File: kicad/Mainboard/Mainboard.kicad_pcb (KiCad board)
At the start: 2 copper layers, 46.9 x 107.1 mm, 277 parts, among them J10 MIC_EXT, J11 VIB2, J12 SPK_EXT, J13 GPS_CONN, J14 Micro_SD_Card, J15 DBG_CONN, J3 USB_OTG, J4 SWD, J5 BATT, J6 POT_PWR_SW, J7 Conn_01x10, J8 Antenna, J9 VIB1, Q1 BSS138, Q2 BSS138, Q3 BGA6589, Q4 BSS138, Q5 BSS138, Q6 BSS138, Q7 FDV304P, SW1 INT_PTT_SW, T1 AFT05MS004NT1, U1 STM32F777VIT, U10 LM386, U11 LSM9DS1, U12 GD25Q16CSIGTR, U13 BGA2874, U14 ESP8266EX, U2 USBLC6-2SC6, U3 LD1117S50TR_SOT223, U4 LD1117S33TR_SOT223, U5 ADF7021, U6 HMC546MS8GETR, U7 LM2904A, U8 HEF4066B, U9 OPA340UA, X1 12.288MHz, Y1 24MHz

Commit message: few fixes
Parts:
- moved C26 1.53 mm to (44.4, 101.9), turned to 180 degrees
- moved JC6 0.53 mm to (27.1, 96.1)
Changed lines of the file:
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@@
   )
   (setup
-    (last_trace_width 1)
+    (last_trace_width 0.25)
     (user_trace_width 0.2)
     (user_trace_width 0.25)
@@
   )
   (module TR-9:Pad1x3 (layer F.Cu)
-    (at 27.0891 95.5421 90)
-    (fp_text reference JC6 (at 0.2794 3.3147 90) (layer F.SilkS)
-      (effects (font (size 1 1) (thickness 0.15)))
+    (at 27.0891 96.0755 90)
+    (fp_text reference JC6 (at 0.3175 3.1115 270) (layer F.SilkS)
+      (effects (font (size 0.5 0.5) (thickness 0.15)))
     )
     (fp_text value Batt (at 0 -0.5 90) (layer F.Fab)
@@
     (at 48.8061 98.6028 90)
     (fp_text reference JC5 (at 0 0.5 90) (layer F.SilkS)
-      (effects (font (size 1 1) (thickness 0.15)))
+      (effects (font (size 0.5 0.5) (thickness 0.15)))
     )
     (fp_text value 5V (at 0 -0.5 90) (layer F.Fab)
@@
   (module TR-9:Pad1x3 (layer F.Cu)
     (at 24.826385 97.580573 135)
-    (fp_text reference JC4 (at -1.873792 -0.002908 135) (layer F.SilkS)
-      (effects (font (size 1 1) (thickness 0.15)))
+    (fp_text reference JC4 (at -0.634517 0.338342 135) (layer F.SilkS)
+      (effects (font (size 0.5 0.5) (thickness 0.15)))
     )
     (fp_text value Batt (at 0 -0.5 135) (layer F.Fab)
@@
     (at 32.8676 90.4494)
     (fp_text reference JC3 (at 0 0.5) (layer F.SilkS)
-      (effects (font (size 1 1) (thickness 0.15)))
+      (effects (font (size 0.5 0.5) (thickness 0.15)))
     )
     (fp_text value Batt (at 0 -0.5) (layer F.Fab)
@@
     (at 55.9811 99.0346)
     (fp_text reference JC2 (at 0 0.5) (layer F.SilkS)
-      (effects (font (size 1 1) (thickness 0.15)))
+      (effects (font (size 0.5 0.5) (thickness 0.15)))
     )
     (fp_text value Batt (at 0 -0.5) (layer F.Fab)
@@
     (at 23.1394 94.234 180)
     (fp_text reference JC1 (at 2.729998 1.634407 180) (layer F.SilkS)
-      (effects (font (size 1 1) (thickness 0.15)))
+      (effects (font (size 0.5 0.5) (thickness 0.15)))
     )
     (fp_text value Batt (at 0 -0.499999 180) (layer F.Fab)
@@
     (at 35.6108 86.0298 90)
     (fp_text reference L8 (at 0 3.937 90) (layer F.SilkS)
-      (effects (font (size 1 1) (thickness 0.15)))
+      (effects (font (size 0.5 0.5) (thickness 0.15)))
     )
     (fp_text value 8/0.5/2.4 (at 0.889 -4.31 90) (layer F.Fab)
@@
     (attr virtual)
     (fp_text reference H4 (at 0 -2.9) (layer F.SilkS)
-      (effects (font (size 1 1) (thickness 0.15)))
+      (effects (font (size 0.5 0.5) (thickness 0.15)))
     )
     (fp_text value MountingHole_Pad (at 0 2.9) (layer F.Fab)
@@
     (attr virtual)
     (fp_text reference H1 (at 0 -2.9) (layer F.SilkS)
-      (effects (font (size 1 1) (thickness 0.15)))
+      (effects (font (size 0.5 0.5) (thickness 0.15)))
     )
     (fp_text value MountingHole_Pad (at 0 2.9) (layer F.Fab)
@@
   )
   (module Capacitor_SMD:C_0603_1608Metric (layer F.Cu)
-    (at 45.9105 102.2477 292.5)
+    (at 44.4246 101.8794 180)
     (descr "Capacitor SMD 0603 (1608 Metric), square (rectangular) end terminal, IPC_7351 nominal, (Body size source: http://www.tortai-tech.com/upload/download/2011102023233369053.pdf), generated with kicad-footprint-generator")
     (tags capacitor)
     (attr smd)
-    (fp_text reference C26 (at 0 -1.43 112.5) (layer F.SilkS)
+    (fp_text reference C26 (at 0 -1.43) (layer F.SilkS)
       (effects (font (size 0.5 0.5) (thickness 0.15)))
     )
-    (fp_text value 10n (at 0 1.43 112.5) (layer F.Fab)
+    (fp_text value 10n (at 0 1.43) (layer F.Fab)
       (effects (font (size 1 1) (thickness 0.15)))
     )
-    (fp_text user %R (at 0 0 112.5) (layer F.Fab)
+    (fp_text user %R (at 0 0) (layer F.Fab)
       (effects (font (size 0.4 0.4) (thickness 0.06)))
     )
@@
     (fp_line (start -0.8 -0.4) (end 0.8 -0.4) (layer F.Fab) (width 0.1))
     (fp_line (start -0.8 0.4) (end -0.8 -0.4) (layer F.Fab) (width 0.1))
-    (pad 2 smd roundrect (at 0.7875 0 292.5) (size 0.875 0.95) (layers F.Cu F.Paste F.Mask) (roundrect_rratio 0.25)
+    (pad 2 smd roundrect (at 0.7875 0 180) (size 0.875 0.95) (layers F.Cu F.Paste F.Mask) (roundrect_rratio 0.25)
       (net 1 GND))
-    (pad 1 smd roundrect (at -0.7875 0 292.5) (size 0.875 0.95) (layers F.Cu F.Paste F.Mask) (roundrect_rratio 0.25)
+    (pad 1 smd roundrect (at -0.7875 0 180) (size 0.875 0.95) (layers F.Cu F.Paste F.Mask) (roundrect_rratio 0.25)
       (net 12 +3V3))
     (model ${KISYS3DMOD}/Capacitor_SMD.3dshapes/C_0603_1608Metric.wrl
@@
     (tags "test point SMD pad")
     (attr virtual)
-    (fp_text reference TP3 (at 0 -1.448) (layer F.SilkS)
+    (fp_text reference TP3 (at 0.1778 1.1303) (layer F.SilkS)
       (effects (font (size 0.5 0.5) (thickness 0.15)))
     )
@@
     (tags "test point SMD pad")
     (attr virtual)
-    (fp_text reference TP1 (at -1.2573 0.6223) (layer F.SilkS)
+    (fp_text reference TP1 (at -0.1397 1.1176) (layer F.SilkS)
       (effects (font (size 0.5 0.5) (thickness 0.15)))
     )
@@
     (tags resistor)
     (attr smd)
-    (fp_text reference R14 (at -1.7019 0.127 270) (layer F.SilkS)
+    (fp_text reference R14 (at -1.8289 0.2667 270) (layer F.SilkS)
       (effects (font (size 0.5 0.5) (thickness 0.15)))
     )
@@
     (tags resistor)
     (attr smd)
-    (fp_text reference R11 (at 0 -1.43 270) (layer F.SilkS)
+    (fp_text reference R11 (at 0.0127 1.1049 270) (layer F.SilkS)
       (effects (font (size 0.5 0.5) (thickness 0.15)))
     )
@@
     (tags resistor)
     (attr smd)
-    (fp_text reference R9 (at 1.0668 -1.0922 270) (layer F.SilkS)
+    (fp_text reference R9 (at 1.9431 0.0127) (layer F.SilkS)
       (effects (font (size 0.5 0.5) (thickness 0.15)))
     )
@@
     (tags capacitor)
     (attr smd)
-    (fp_text reference C45 (at -0.1017 -1.0414 90) (layer F.SilkS)
+    (fp_text reference C45 (at -1.994 -0.0762 180) (layer F.SilkS)
       (effects (font (size 0.5 0.5) (thickness 0.15)))
     )
@@
     (tags capacitor)
     (attr smd)
-    (fp_text reference C44 (at -0.4319 1.0922 90) (layer F.SilkS)
+    (fp_text reference C44 (at -0.2414 1.3208 90) (layer F.SilkS)
       (effects (font (size 0.5 0.5) (thickness 0.15)))
     )
@@
     (tags capacitor)
     (attr smd)
-    (fp_text reference C39 (at -1.9813 0.0762 -90) (layer F.SilkS)
+    (fp_text reference C39 (at -2.1337 0.2413 -90) (layer F.SilkS)
       (effects (font (size 0.5 0.5) (thickness 0.15)))
     )
@@
     (tags capacitor)
     (attr smd)
-    (fp_text reference C38 (at 1.8797 -0.5842 270) (layer F.SilkS)
+    (fp_text reference C38 (at 2.1083 -0.4953) (layer F.SilkS)
       (effects (font (size 0.5 0.5) (thickness 0.15)))
     )
@@
     (tags capacitor)
     (attr smd)
-    (fp_text reference C37 (at -2.0321 0.0762 90) (layer F.SilkS)
+    (fp_text reference C37 (at -1.105 1.1049 180) (layer F.SilkS)
       (effects (font (size 0.5 0.5) (thickness 0.15)))
     )
@@
     (tags capacitor)
     (attr smd)
-    (fp_text reference C32 (at 0.0761 0.9144) (layer F.SilkS)
+    (fp_text reference C32 (at 1.3209 -1.0668) (layer F.SilkS)
       (effects (font (size 0.5 0.5) (thickness 0.15)))
     )
@@
     (tags capacitor)
     (attr smd)
-    (fp_text reference C31 (at 0 -1.43 270) (layer F.SilkS)
+    (fp_text reference C31 (at 0.5333 -1.0668 270) (layer F.SilkS)
       (effects (font (size 0.5 0.5) (thickness 0.15)))
     )
@@
     (tags capacitor)
     (attr smd)
-    (fp_text reference C30 (at -1.7271 -0.5588 180) (layer F.SilkS)
+    (fp_text reference C30 (at -1.5874 -0.7239 180) (layer F.SilkS)
       (effects (font (size 0.5 0.5) (thickness 0.15)))
     )
@@
     (tags capacitor)
     (attr smd)
-    (fp_text reference C29 (at -1.6763 0 270) (layer F.SilkS)
+    (fp_text reference C29 (at -0.8129 1.016) (layer F.SilkS)
       (effects (font (size 0.5 0.5) (thickness 0.15)))
     )
@@
     (descr "tactile switch 6mm ALPS SKHH right angle http://www.alps.com/prod/info/E/HTML/Tact/SnapIn/SKHH/SKHHLUA010.html")
     (tags "tactile switch 6mm ALPS SKHH right angle")
-    (fp_text reference SW1 (at 5.6484 4.8368 270) (layer F.SilkS)
+    (fp_text reference SW1 (at 3.9339 2.9064) (layer F.SilkS)
       (effects (font (size 0.5 0.5) (thickness 0.15)))
     )
@@
   (via (at 34.6202 94.361) (size 0.4) (drill 0.3) (layers F.Cu B.Cu) (net 1))
   (via (at 33.8328 94.361) (size 0.4) (drill 0.3) (layers F.Cu B.Cu) (net 1))
-  (via (at 28.1686 97.5741) (size 0.4) (drill 0.3) (layers F.Cu B.Cu) (net 1))
+  (via (at 28.2448 98.2345) (size 0.4) (drill 0.3) (layers F.Cu B.Cu) (net 1))
   (via (at 55.245 162.0012) (size 0.4) (drill 0.3) (layers F.Cu B.Cu) (net 1))
   (via (at 57.15 162.0012) (size 0.4) (drill 0.3) (layers F.Cu B.Cu) (net 1))

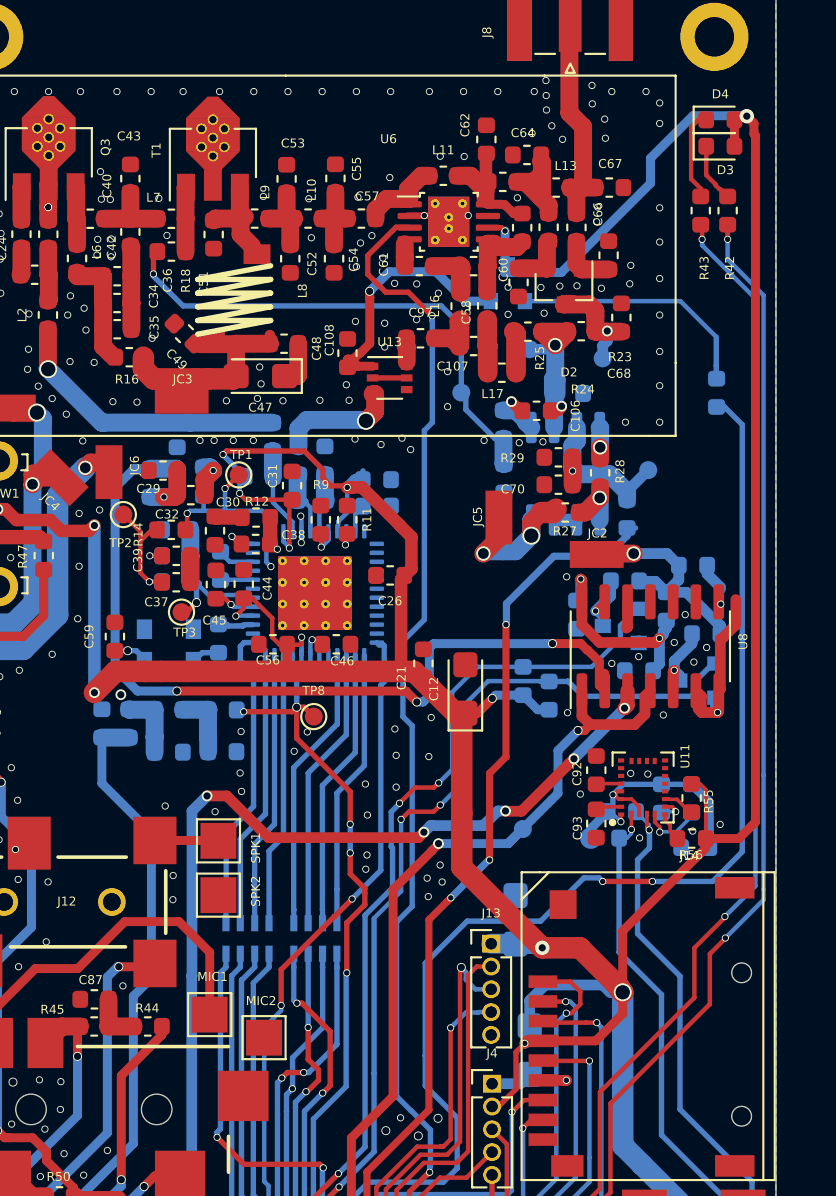
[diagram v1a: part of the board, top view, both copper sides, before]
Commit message: more jumper added
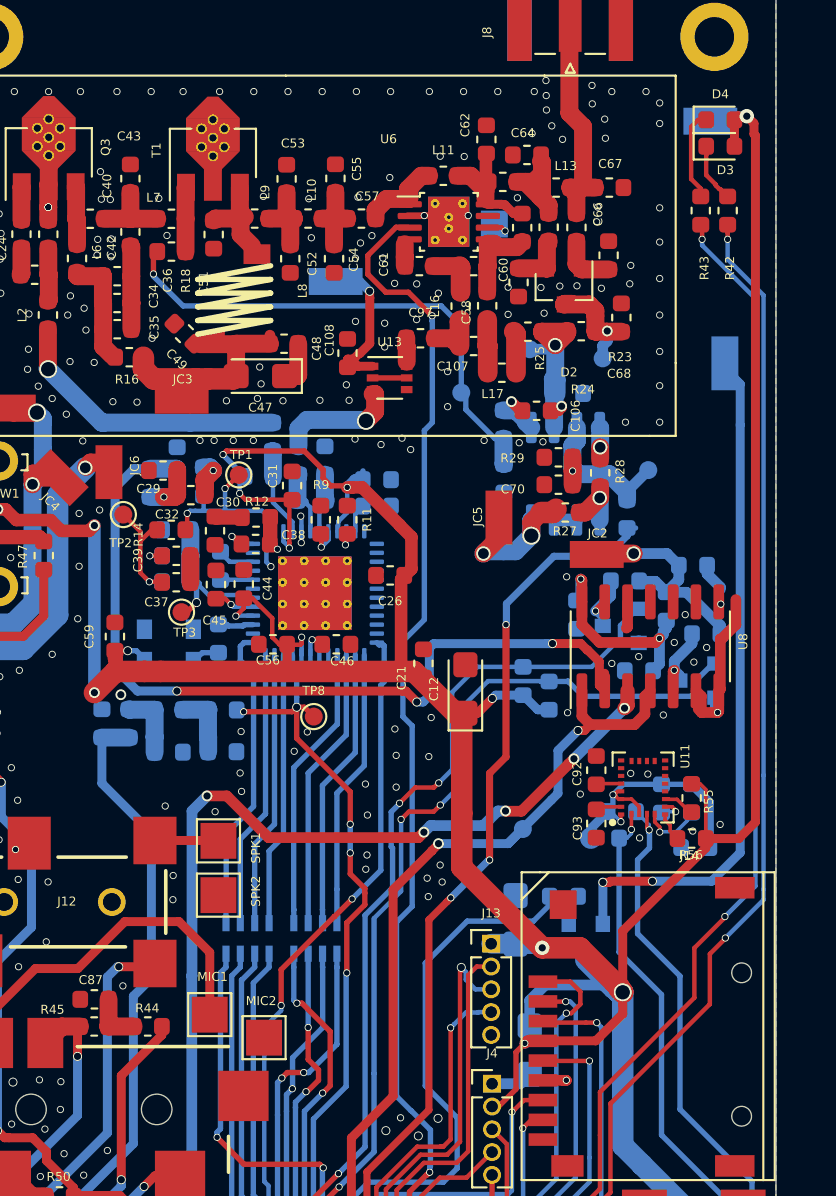
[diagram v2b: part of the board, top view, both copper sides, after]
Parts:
- added JC10: TRX_SW_PWR_2, TR-9:Pad1x3, B.Cu at (62.3, 78.3)
- added JC7: LNA_1, TR-9:Pad1x3, B.Cu at (64.7, 90.0)
- added JC8: LNA_2, TR-9:Pad1x3, B.Cu at (41.4, 87.2)
- added JC9: TRX_SW_PWR_1, TestPoint:TestPoint_Pad_1.5x1.5mm, B.Cu at (50.2, 82.3)
- moved Q7 36.9 mm to (55.3, 122.3), turned to 270 degrees
- moved R20 29.3 mm to (54.1, 119.7), turned to 0 degrees
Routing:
- net LNA_On: track 68.1 -> 30.4 mm, vias 2 -> 0
- net Net-(C108-Pad1): track 14.4 -> 48.6 mm, vias 1 -> 3
- net Net-(Q7-Pad1): track 14.5 -> 1.75 mm
- net +3V3: track 492.8 -> 480.2 mm

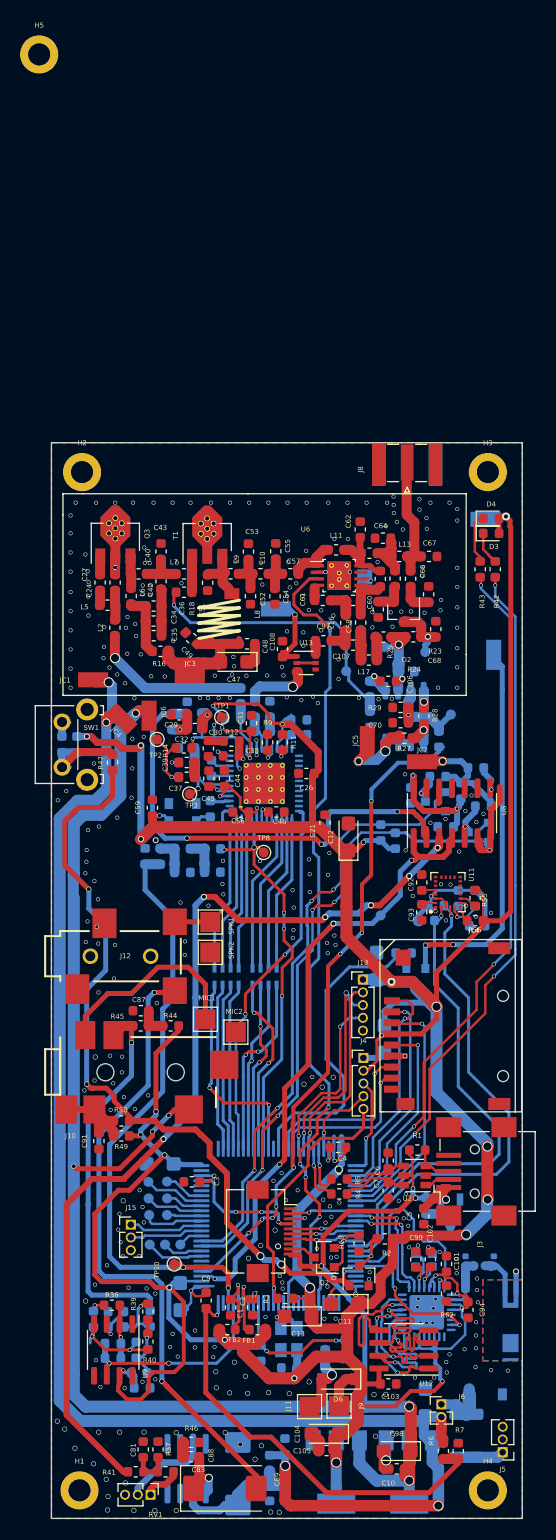
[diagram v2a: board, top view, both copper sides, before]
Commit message: removed ESP8266 and it's circuitry; instead added a Pin Headers 2x4 for soldering in ESP8266 SoM; changed vias to manufacturable by JlcPcb; plotted PDF
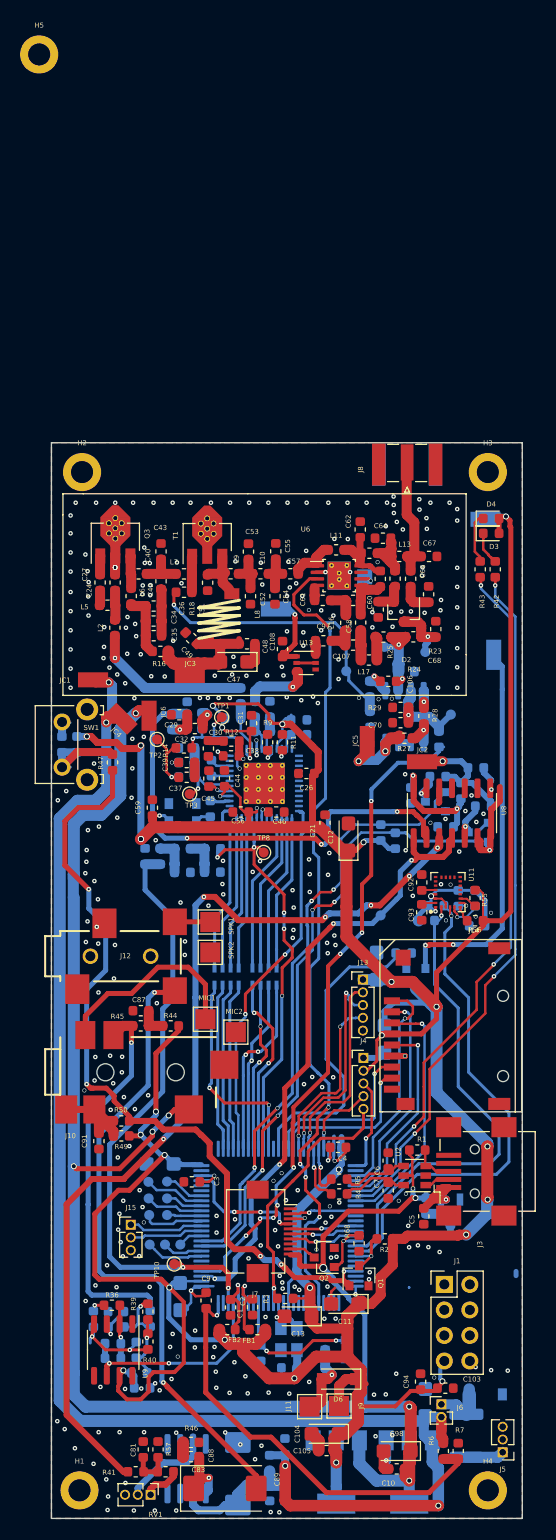
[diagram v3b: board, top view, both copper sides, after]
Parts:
- removed AE1: Antenna_Chip, TR-9:RFECA3216060A1T_shifted
- removed C100: 5p6, Inductor_SMD:L_0402_1005Metric
- removed C101: 100n, Capacitor_SMD:C_0603_1608Metric
- removed C102, C99: 10p, Capacitor_SMD:C_0603_1608Metric
- removed the C104 at (63.1, 150.4)
- removed the C105 at (60.3, 150.4)
- removed L15: L, Inductor_SMD:L_0402_1005Metric
- removed R62: 12k, Resistor_SMD:R_0603_1608Metric
- removed U12: GD25Q16CSIGTR, Package_SO:SOIC-8_3.9x4.9mm_P1.27mm
- removed U14: ESP8266EX, Package_DFN_QFN:QFN-32-1EP_5x5mm_P0.5mm_EP3.45x3.45mm
- removed Y1: 24MHz, Crystal:Crystal_SMD_Abracon_ABM10-4Pin_2.5x2.0mm
- added J1: Conn_02x04_Odd_Even, Connector_PinHeader_2.54mm:PinHeader_2x04_P2.54mm_Vertical, F.Cu at (58.2, 152.7)
- C94: value 10u -> 10n
- moved C94 8.55 mm to (55.8, 162.4), turned to 90 degrees
- moved C103 5.69 mm to (58.3, 163.1)
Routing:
- net +3V3: track 480.2 -> 449.3 mm, vias 38 -> 35
- net WIFI_RST: track 20.2 -> 0.80 mm
- net WIFI_EN: track 15.1 -> 0.00 mm, vias 2 -> 0
- net MEM_D3: track 14.2 -> 0.00 mm, vias 1 -> 0
- net MEM_D1: track 13.8 -> 0.00 mm, vias 1 -> 0
- net MEM_D0: track 13.8 -> 0.00 mm, vias 1 -> 0
- net MEM_D2: track 13.4 -> 0.00 mm, vias 1 -> 0
- net MEM_CS: track 13.3 -> 0.00 mm, vias 3 -> 0
- net MEM_CLK: track 13.2 -> 0.00 mm, vias 1 -> 0
- net UART2_TX: track 12.2 -> 0.04 mm, vias 2 -> 1
- net UART2_RX: track 12.2 -> 0.45 mm, vias 2 -> 0
- net Net-(C99-Pad1): track 5.66 -> 0.00 mm, vias 1 -> 0
- net Net-(AE1-Pad1): track 4.34 -> 0.00 mm
- net Net-(C102-Pad1): track 4.03 -> 0.00 mm, vias 1 -> 0
- net Net-(C100-Pad2): track 3.15 -> 0.00 mm
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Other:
- rule via_min_drill: 0.3 -> 0.1

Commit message: changed BATT cap
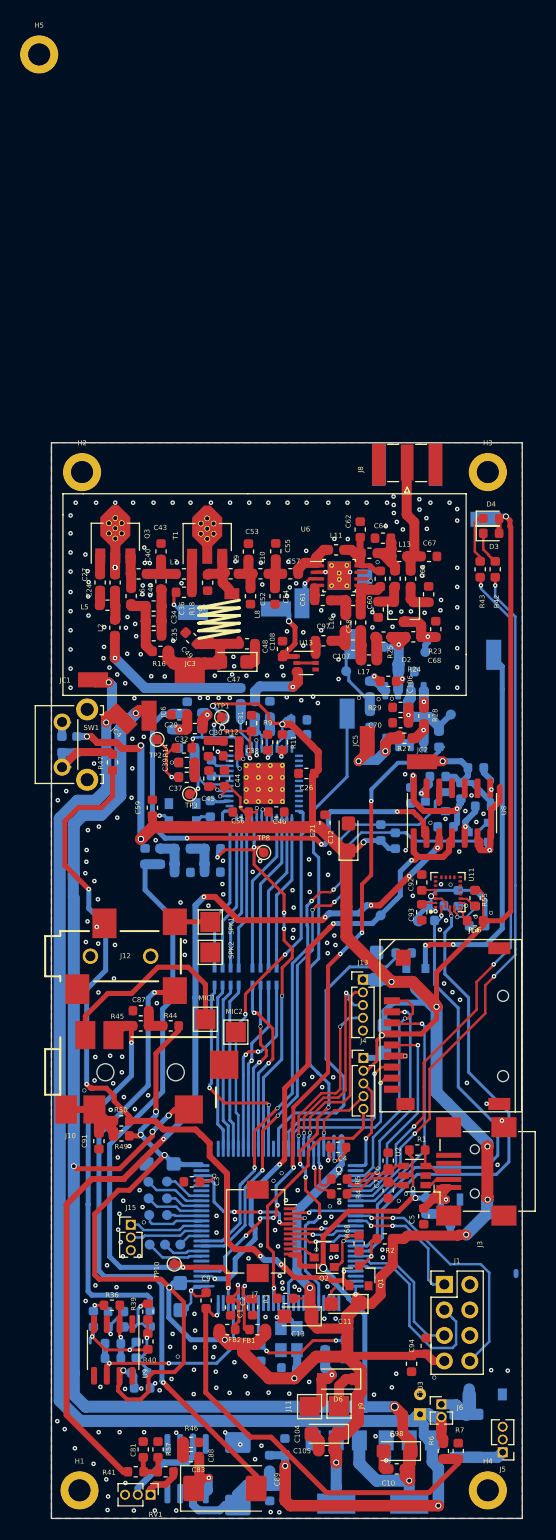
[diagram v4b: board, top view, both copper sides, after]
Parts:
- added JC11: BIAS, TR-9:Pad1x3, B.Cu at (33.2, 87.5)
- added JC12: BIAS, TR-9:Pad1x3, B.Cu at (50.7, 89.0)
- added JC13: TRX_SW, TR-9:Pad1x3, B.Cu at (45.7, 84.9)
- added JC14: TRX_SW, TR-9:Pad1x3, B.Cu at (46.8, 96.0)
- C8: footprint Capacitor_Tantalum_SMD:CP_EIA-3216-18_Kemet-A -> Capacitor_THT:CP_Radial_D4.0mm_P2.00mm
- J1: value Conn_02x04_Odd_Even -> ESP8266 module
- moved C103 4.15 mm to (54.9, 160.6), turned to 270 degrees
- moved C94 3.60 mm to (56.3, 158.9)
- moved C8 1.28 mm to (55.7, 165.7)
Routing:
- net UART2_TX: track 0.04 -> 25.2 mm, vias 1 -> 2
- net WIFI_EN: track 0.00 -> 19.9 mm
- net Net-(JC11-Pad1): track 28.5 -> 13.5 mm
- net WIFI_RST: track 0.80 -> 15.0 mm
- net UART2_RX: track 0.45 -> 13.7 mm, vias 0 -> 2
- net TRX_SW: track 81.2 -> 68.4 mm
- net +BATT: track 179.4 -> 180.9 mm
- net +3V3: track 449.3 -> 448.1 mm, vias 35 -> 34
- net +5V: track 200.4 -> 199.6 mm
- net Net-(C108-Pad1): track 48.6 -> 47.9 mm
- net BOOT0: track 5.43 -> 5.99 mm
- net GND: vias 328 -> 332

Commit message: some small changes
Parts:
- removed H5: MountingHole_Pad, MountingHole:MountingHole_2.2mm_M2_ISO14580_Pad
- moved C54 0.83 mm to (41.3, 83.4)
- moved C52 0.61 mm to (39.1, 83.7)
- moved C55 0.56 mm to (41.2, 79.2)
- moved C57 0.55 mm to (42.8, 81.5)
- moved L10 0.55 mm to (39.8, 81.5)
- moved C53 0.55 mm to (38.7, 79.2)
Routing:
- net Net-(C52-Pad2): track 4.40 -> 7.94 mm
- net GND: vias 332 -> 337
- net (no net): vias 0 -> 1
